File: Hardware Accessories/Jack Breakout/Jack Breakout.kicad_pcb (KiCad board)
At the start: 2 copper layers, 34.5 x 21.3 mm, 3 parts, among them J1 AudioJack3_Switch, J2 Conn_01x03

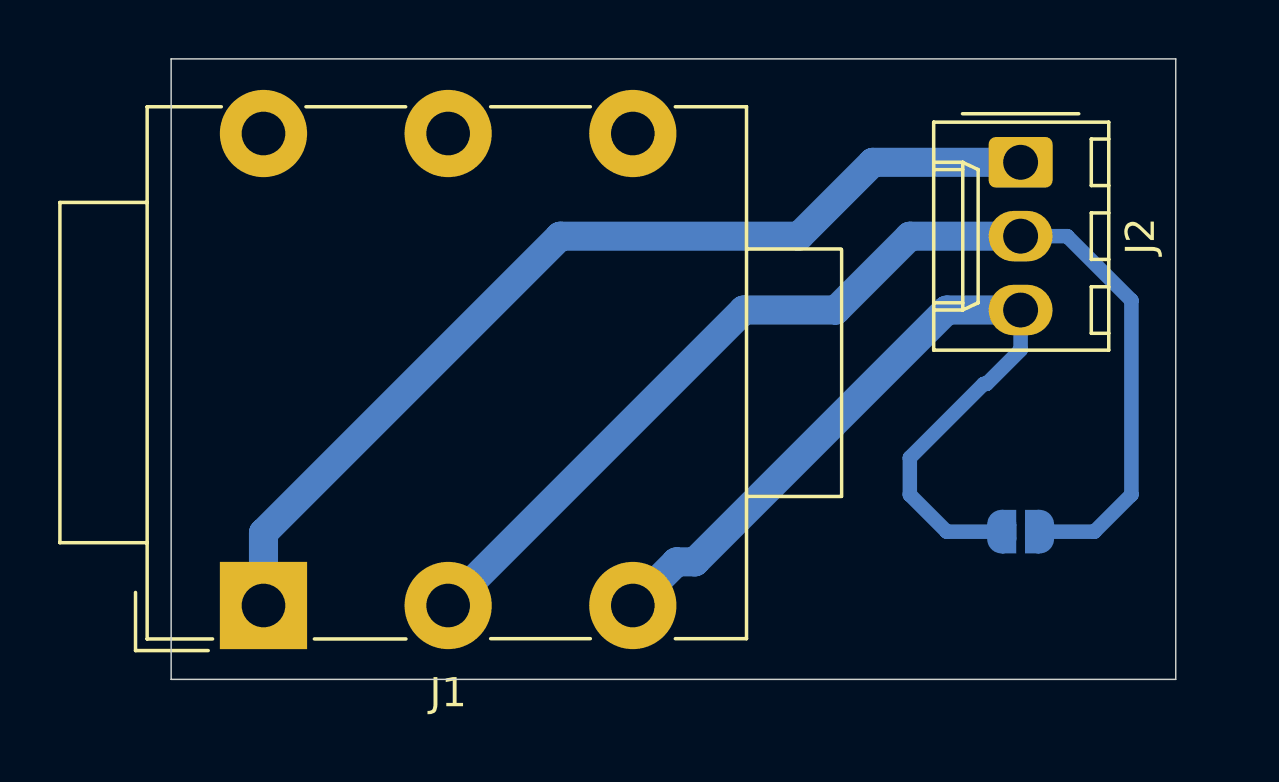
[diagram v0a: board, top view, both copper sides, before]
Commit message: Added .ipynb_checkpoints to .gitignore; finished 1/4" jack connector pending review; started exploratory physical design .ipynb
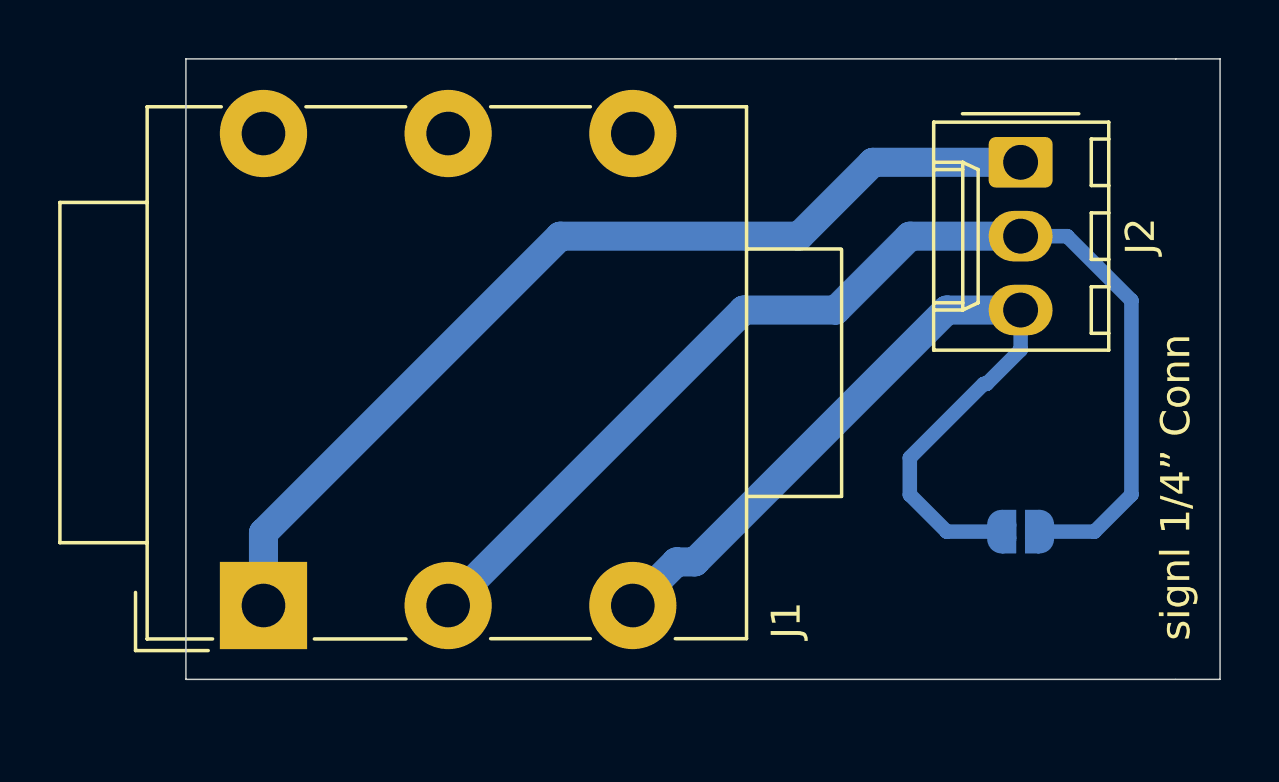
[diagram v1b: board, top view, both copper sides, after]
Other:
- board size 34.5 x 21.3 mm -> 35.6 x 21.3 mm
- board text added: "signl 1/4” Conn"
- board text removed: "NOTE: Check side of jack connector is right"
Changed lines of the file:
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@@
   (general
     (thickness 1.6)
-    (drawings 5)
+    (drawings 8)
     (tracks 25)
     (zones 0)
@@
     (descr "NMJ6HCD2, TRS 1/4in (http://www.neutrik.com/en/audio/plugs-and-jacks/m-series/nmj6hcd2)")
     (tags "NMJ6HCD2 TRS stereo jack connector")
-    (fp_text reference J1 (at 6.35 -3) (layer F.SilkS)
+    (fp_text reference J1 (at -5.27812 -0.508 270) (layer F.SilkS)
       (effects (font (size 1 1) (thickness 0.15)))
     )
@@
     (tags "solder jumper open")
     (attr virtual)
-    (fp_text reference JP1 (at 0 1.8) (layer B.SilkS)
-      (effects (font (size 1 1) (thickness 0.15)) (justify mirror))
+    (fp_text reference JP1 (at 0 -2.54 90) (layer F.SilkS) hide
+      (effects (font (size 1 1) (thickness 0.15)))
     )
     (fp_text value SolderJumper_2_Open (at 2.54 0 90) (layer B.Fab)
@@
       ))
   )
-  (gr_text "NOTE: Check side of jack connector is right" (at 40.132 50.292) (layer Dwgs.User)
+  (gr_line (start 58.928 24.384) (end 57.404 24.384) (layer Edge.Cuts) (width 0.05))
+  (gr_line (start 57.404 45.72) (end 58.928 45.72) (layer Edge.Cuts) (width 0.05))
+  (gr_text "signl 1/4” Conn" (at 57.404 39.116 90) (layer F.SilkS)
     (effects (font (size 1 1) (thickness 0.15)))
   )
-  (gr_line (start 22.86 45.72) (end 22.86 24.384) (layer Edge.Cuts) (width 0.05))
-  (gr_line (start 57.404 45.72) (end 22.86 45.72) (layer Edge.Cuts) (width 0.05))
-  (gr_line (start 57.404 24.384) (end 57.404 45.72) (layer Edge.Cuts) (width 0.05))
-  (gr_line (start 22.86 24.384) (end 57.404 24.384) (layer Edge.Cuts) (width 0.05))
+  (gr_text "signl 1/4” Conn" (at 57.404 39.116 90) (layer F.Cu)
+    (effects (font (size 1 1) (thickness 0.15)))
+  )
+  (gr_line (start 23.368 45.72) (end 23.368 24.384) (layer Edge.Cuts) (width 0.05))
+  (gr_line (start 57.404 45.72) (end 23.368 45.72) (layer Edge.Cuts) (width 0.05))
+  (gr_line (start 58.928 24.384) (end 58.928 45.72) (layer Edge.Cuts) (width 0.05))
+  (gr_line (start 23.368 24.384) (end 57.404 24.384) (layer Edge.Cuts) (width 0.05))
   (segment (start 52.07 30.48) (end 48.26 30.48) (width 1) (layer B.Cu) (net 4))
   (segment (start 48.26 30.48) (end 45.72 33.02) (width 1) (layer B.Cu) (net 4))
